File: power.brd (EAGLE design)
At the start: 75.9 x 52.1 mm, 15 parts, among them Q1 MOSFET-NCHANNELSMD, Q2 MOSFET-NCHANNELSMD, U1 MCP73831, X1 Micro USB

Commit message: Updating with changes
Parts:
- removed C3, C4: 4.7uF, SparkFun:0402-CAP
- removed Q1, Q2: MOSFET-NCHANNELSMD, SparkFun:SOT23-3
- removed R3, R4, R7, R8: 10K, SparkFun:0603-RES
- removed R6: 330, SparkFun:0402-RES
- removed R9: 2K, SparkFun:0402-RES
- added C1, C2: 4.7uF, SparkFun-Capacitors:0805-CAP
- added R2: 2k, SparkFun-Resistors:0805
- R1: value 10k -> 330
- moved R1 31.5 mm to (8.89, 10.2)
- moved JP7 23.3 mm to (21.6, 7.62)
- moved D11 20.5 mm to (14.0, 3.81), turned to 90 degrees
- moved U1 20.5 mm to (8.89, 7.62), turned to 90 degrees
- moved X1 7.62 mm to (2.54, 6.35)
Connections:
- removed net 3.3V: Q1.1, Q2.1, R3.1, R7.1
- removed net RTS: Q2.2, R7.2
- removed net RTS_5V: Q2.3, R8.2
- removed net TX: Q1.2, R3.2
- removed net TX_5V: Q1.3, R4.2
- net GND: now also C1.2, C2.2, R2.1; no longer C3.2, C4.2, R9.2
- net N$12: now also R1.2; no longer R6.1
- net PROG: now also R2.2; no longer R9.1
- net VCC: now also C2.1; no longer C4.1, R4.1, R8.1
- net VIN: now also C1.1, R1.1; no longer C3.1, R6.2
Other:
- board size 75.9 x 52.1 mm -> 31.4 x 17.8 mm

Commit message: More updates
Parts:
- added IC1: CAT4101, User-Submitted:TO263_5
- added JP1: RA 6Pin SMD, SparkFun-Connectors:1X06-SMD
- added U2: Tiny85-20-SMT, SparkFun-DigitalIC:SO08-EIAJ
- moved D11 14.1 mm to (2.54, 12.1)
- moved C1 12.8 mm to (2.54, 1.91), flipped to the bottom
- moved C2 11.6 mm to (2.54, 14.6), flipped to the bottom
- moved JP7 10.9 mm to (11.4, 11.4), flipped to the bottom, turned to 90 degrees
- moved R1 6.63 mm to (2.54, 12.1), flipped to the bottom
- moved R2 6.38 mm to (2.54, 4.45), flipped to the bottom, turned to 180 degrees
- moved U1 5.75 mm to (3.17, 8.26), flipped to the bottom
- moved X1 0.90 mm to (1.91, 5.71)
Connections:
- removed net VCC: C2.1, JP7.2, U1.3
- new net VBAT: C2.1, JP1.6, JP7.2, U1.3
- net GND: now also IC1.3, JP1.1
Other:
- board size 31.4 x 17.8 mm -> 27.6 x 16.5 mm

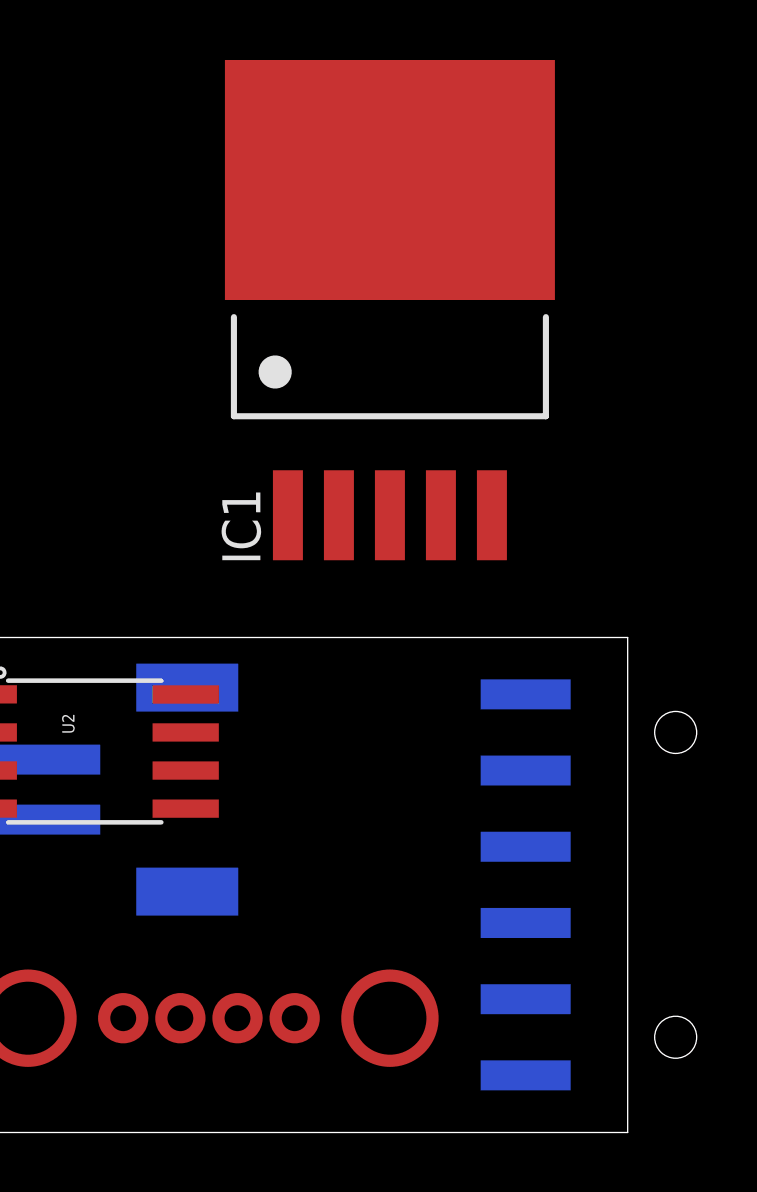
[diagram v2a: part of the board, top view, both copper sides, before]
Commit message: Updated headers to remove annoying holes and now using my own library
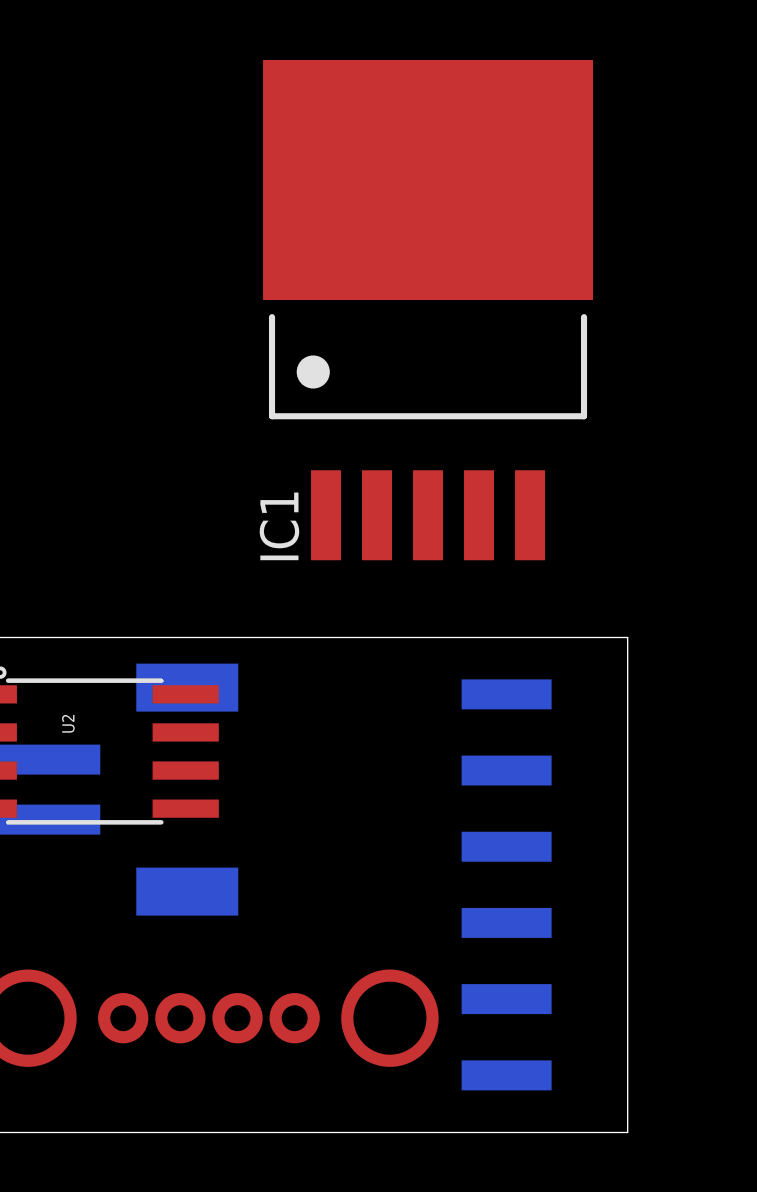
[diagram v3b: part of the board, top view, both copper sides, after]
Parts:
- IC1: value CAT4101 -> UC27775; device User-Submitted:TO263_5 -> mine:TO263_5
- JP1: device SparkFun-Connectors:1X06-SMD -> mine:1X06-SMD-NOHOLES
- moved IC1 1.27 mm to (21.0, 28.6)
- moved JP1 0.64 mm to (28.6, 8.26)
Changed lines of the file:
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@@
 <attribute name="PROD_ID" value="CAP-11625" x="2.54" y="14.605" size="1.778" layer="28" rot="MR0" display="off"/>
-</element>
-<element name="JP1" library="SparkFun-Connectors" package="1X06-SMD" value="RA 6Pin SMD" x="29.21" y="8.255" rot="MR270">
-<attribute name="PROD_ID" value="CONN-08971" x="29.21" y="8.255" size="1.778" layer="28" rot="MR270" display="off"/>
 </element>
 <element name="U2" library="SparkFun-DigitalIC" package="SO08-EIAJ" value="Tiny85-20-SMT" x="9.525" y="12.7" rot="R270">
 <attribute name="PROD_ID" value="IC-09092" x="9.525" y="12.7" size="1.778" layer="27" rot="R270" display="off"/>
 </element>
-<element name="IC1" library="User-Submitted" package="TO263_5" value="CAT4101" x="19.685" y="28.575">
-<attribute name="MF" value="TI" x="19.685" y="28.575" size="0.6096" layer="27" font="vector" display="off"/>
+<element name="JP1" library="mine" package="1X06-SMD-NOHOLES" value="RA 6Pin SMD" x="28.575" y="8.255" rot="MR270">
+<attribute name="PROD_ID" value="CONN-08971" x="28.575" y="8.255" size="1.778" layer="28" rot="MR270" display="off"/>
+</element>
+<element name="IC1" library="mine" package="TO263_5" value="UC27775" x="20.955" y="28.575">
+<attribute name="MF" value="TI" x="20.955" y="28.575" size="1.778" layer="27" display="off"/>
 </element>
 </elements>
@@
 <contactref element="C2" pad="1"/>
 <contactref element="JP1" pad="6"/>
-<wire x1="7.73" y1="12.43" x2="24.21" y2="1.905" width="0" layer="19" extent="16-16"/>
 <wire x1="3.44" y1="14.605" x2="7.73" y2="12.43" width="0" layer="19" extent="16-16"/>
 <wire x1="1.8749" y1="9.205" x2="3.44" y2="14.605" width="0" layer="19" extent="16-16"/>
+<wire x1="23.575" y1="1.905" x2="7.73" y2="12.43" width="0" layer="19" extent="1-16"/>
 </signal>
 <signal name="VIN">
@@
 <contactref element="C1" pad="2"/>
 <contactref element="C2" pad="2"/>
+<contactref element="IC1" pad="3"/>
 <contactref element="JP1" pad="1"/>
-<contactref element="IC1" pad="3"/>
-<wire x1="7.73" y1="10.43" x2="24.21" y2="14.605" width="0" layer="19" extent="16-16"/>
 <wire x1="1.8749" y1="8.255" x2="7.73" y2="10.43" width="0" layer="19" extent="16-16"/>
 <wire x1="1.64" y1="4.445" x2="1.8749" y2="8.255" width="0" layer="19" extent="16-16"/>
 <wire x1="1.64" y1="1.905" x2="1.64" y2="4.445" width="0" layer="19" extent="16-16"/>
 <wire x1="4.555" y1="4.415" x2="1.64" y2="4.445" width="0" layer="19" extent="1-16"/>
+<wire x1="23.575" y1="14.605" x2="1.64" y2="1.905" width="0" layer="19" extent="1-16"/>
 <wire x1="1.64" y1="14.605" x2="1.8749" y2="8.255" width="0" layer="19" extent="16-16"/>
-<wire x1="19.685" y1="20.575" x2="1.64" y2="1.905" width="0" layer="19" extent="1-16"/>
+<wire x1="20.955" y1="20.575" x2="23.575" y2="14.605" width="0" layer="19" extent="1-1"/>
 </signal>
 <signal name="N$12">

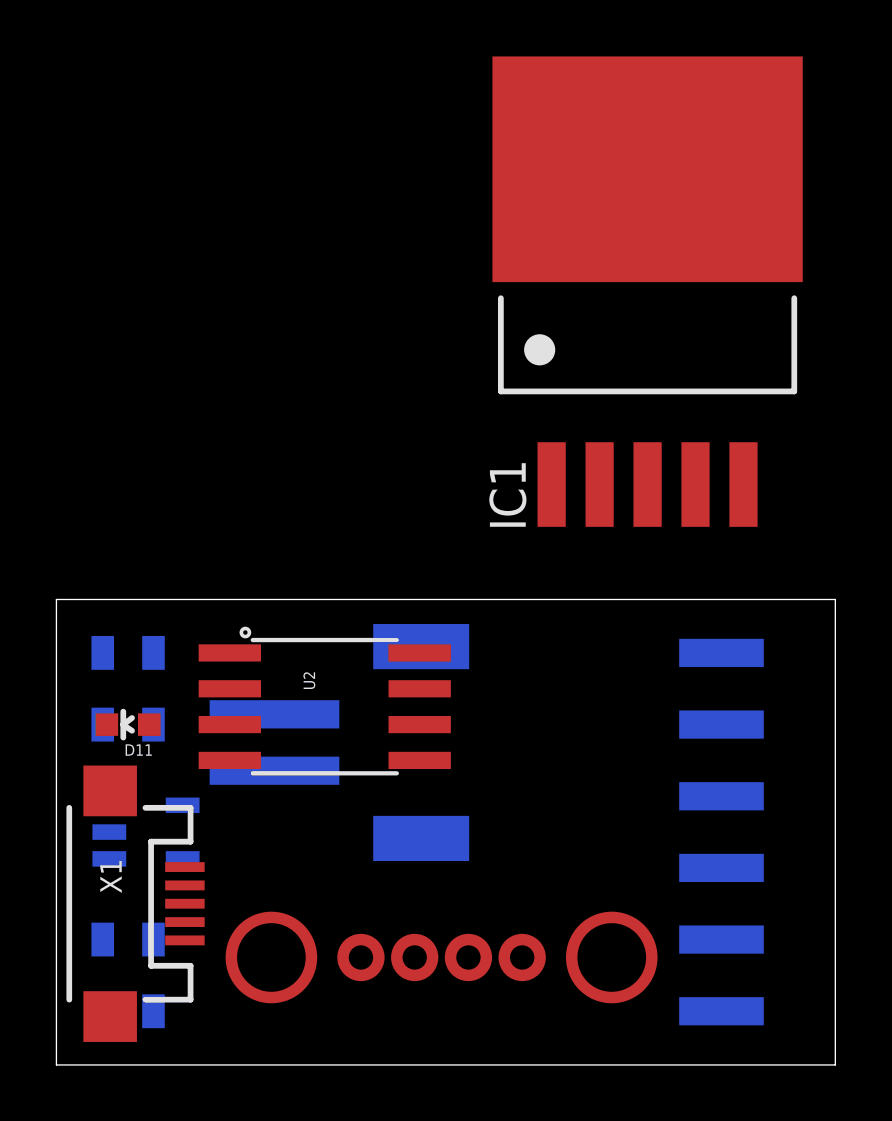
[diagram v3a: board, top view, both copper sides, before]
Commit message: Updated height of board to match bt board and rearranged components
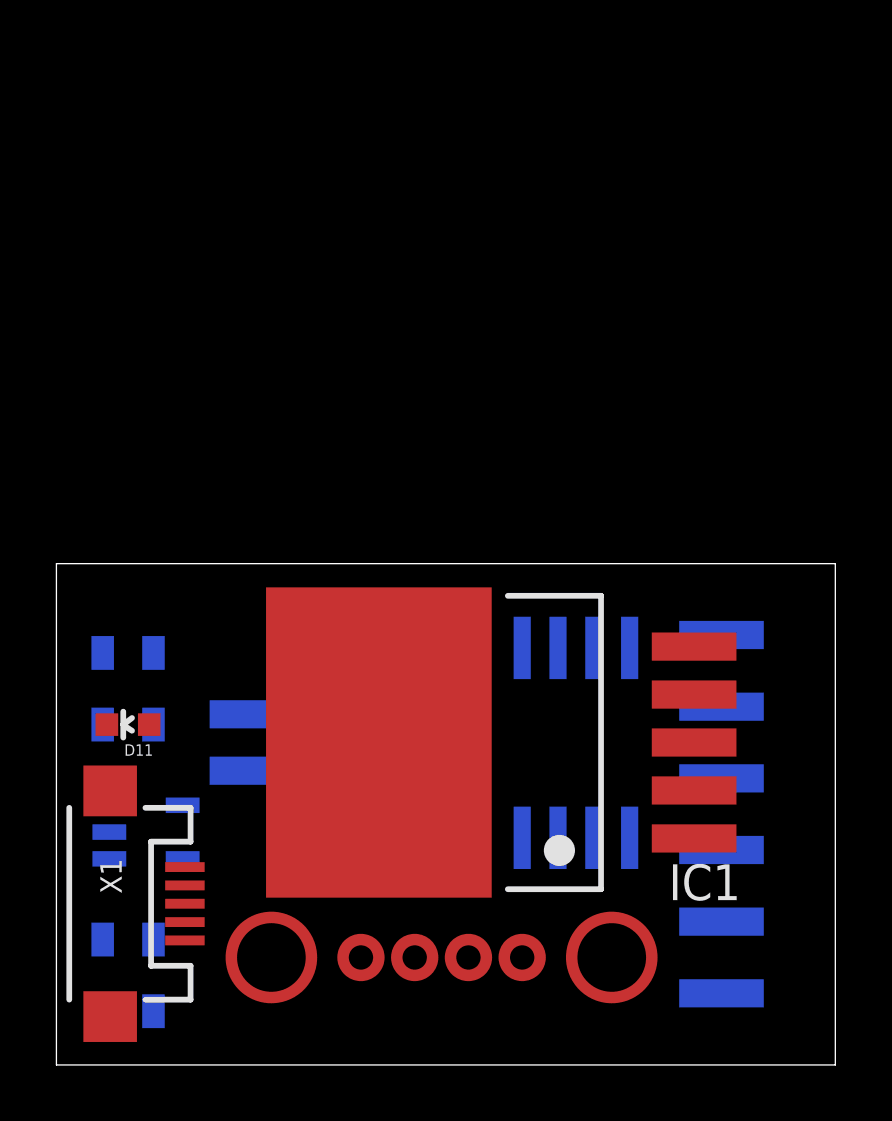
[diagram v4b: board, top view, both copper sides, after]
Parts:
- moved IC1 18.3 mm to (14.6, 11.4), turned to 90 degrees
- moved U2 8.98 mm to (18.4, 11.4), flipped to the bottom, turned to 0 degrees
- moved JP1 0.63 mm to (28.6, 8.89)
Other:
- board size 27.6 x 16.5 mm -> 27.6 x 17.8 mm
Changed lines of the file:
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@@
 <plain>
 <wire x1="0" y1="0" x2="27.61" y2="0" width="0" layer="20"/>
-<wire x1="27.61" y1="0" x2="27.61" y2="16.5" width="0" layer="20"/>
-<wire x1="27.61" y1="16.5" x2="0" y2="16.5" width="0" layer="20"/>
-<wire x1="0" y1="16.5" x2="0" y2="0" width="0" layer="20"/>
+<wire x1="27.61" y1="0" x2="27.61" y2="17.77" width="0" layer="20"/>
+<wire x1="27.61" y1="17.77" x2="0" y2="17.77" width="0" layer="20"/>
+<wire x1="0" y1="17.77" x2="0" y2="0" width="0" layer="20"/>
 <circle x="14.605" y="3.81" radius="0.635" width="0.4064" layer="1"/>
 <circle x="12.7" y="3.81" radius="0.635" width="0.4064" layer="1"/>
@@
 <attribute name="PROD_ID" value="CAP-11625" x="2.54" y="14.605" size="1.778" layer="28" rot="MR0" display="off"/>
 </element>
-<element name="U2" library="SparkFun-DigitalIC" package="SO08-EIAJ" value="Tiny85-20-SMT" x="9.525" y="12.7" rot="R270">
-<attribute name="PROD_ID" value="IC-09092" x="9.525" y="12.7" size="1.778" layer="27" rot="R270" display="off"/>
-</element>
-<element name="JP1" library="mine" package="1X06-SMD-NOHOLES" value="RA 6Pin SMD" x="28.575" y="8.255" rot="MR270">
-<attribute name="PROD_ID" value="CONN-08971" x="28.575" y="8.255" size="1.778" layer="28" rot="MR270" display="off"/>
-</element>
-<element name="IC1" library="mine" package="TO263_5" value="UC27775" x="20.955" y="28.575">
-<attribute name="MF" value="TI" x="20.955" y="28.575" size="1.778" layer="27" display="off"/>
+<element name="U2" library="SparkFun-DigitalIC" package="SO08-EIAJ" value="Tiny85-20-SMT" x="18.415" y="11.43" rot="MR0">
+<attribute name="PROD_ID" value="IC-09092" x="18.415" y="11.43" size="1.778" layer="28" rot="MR0" display="off"/>
+</element>
+<element name="JP1" library="mine" package="1X06-SMD-NOHOLES" value="RA 6Pin SMD" x="28.575" y="8.89" rot="MR270">
+<attribute name="PROD_ID" value="CONN-08971" x="28.575" y="8.89" size="1.778" layer="28" rot="MR270" display="off"/>
+</element>
+<element name="IC1" library="mine" package="TO263_5" value="UC27775" x="14.605" y="11.43" rot="R90">
+<attribute name="MF" value="TI" x="14.605" y="11.43" size="1.778" layer="27" rot="R90" display="off"/>
 </element>
 </elements>
@@
 <wire x1="3.44" y1="14.605" x2="7.73" y2="12.43" width="0" layer="19" extent="16-16"/>
 <wire x1="1.8749" y1="9.205" x2="3.44" y2="14.605" width="0" layer="19" extent="16-16"/>
-<wire x1="23.575" y1="1.905" x2="7.73" y2="12.43" width="0" layer="19" extent="1-16"/>
+<wire x1="23.575" y1="2.54" x2="7.73" y2="12.43" width="0" layer="19" extent="1-16"/>
 </signal>
 <signal name="VIN">
@@
 <wire x1="1.64" y1="1.905" x2="1.64" y2="4.445" width="0" layer="19" extent="16-16"/>
 <wire x1="4.555" y1="4.415" x2="1.64" y2="4.445" width="0" layer="19" extent="1-16"/>
-<wire x1="23.575" y1="14.605" x2="1.64" y2="1.905" width="0" layer="19" extent="1-16"/>
+<wire x1="23.575" y1="15.24" x2="1.64" y2="1.905" width="0" layer="19" extent="1-16"/>
 <wire x1="1.64" y1="14.605" x2="1.8749" y2="8.255" width="0" layer="19" extent="16-16"/>
-<wire x1="20.955" y1="20.575" x2="23.575" y2="14.605" width="0" layer="19" extent="1-1"/>
+<wire x1="22.605" y1="11.43" x2="23.575" y2="15.24" width="0" layer="19" extent="1-1"/>
 </signal>
 <signal name="N$12">
